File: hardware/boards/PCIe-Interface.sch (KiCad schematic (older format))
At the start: 0 parts

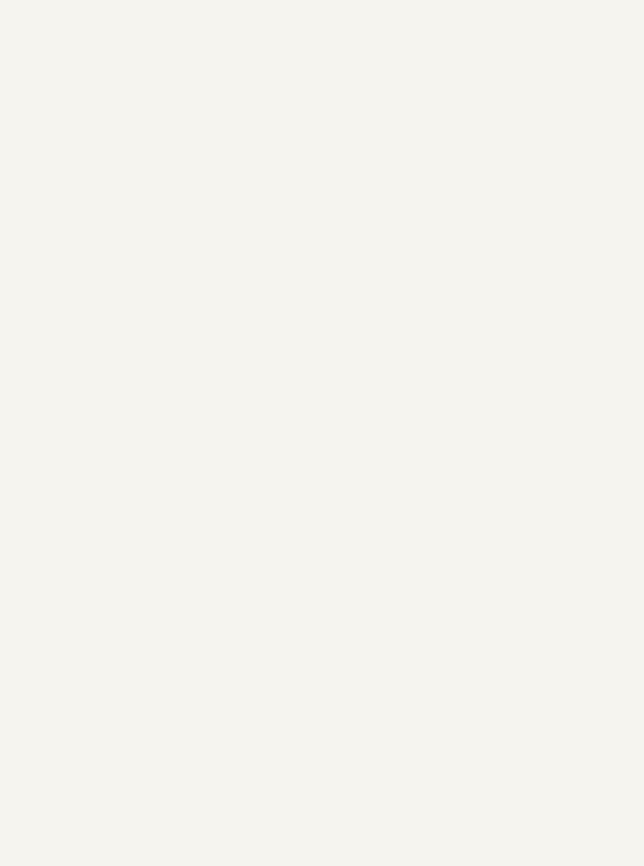
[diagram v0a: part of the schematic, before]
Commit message: Added some more schematics for blocking things out, and tweaked the GND fingers on the PCIe edge a bit
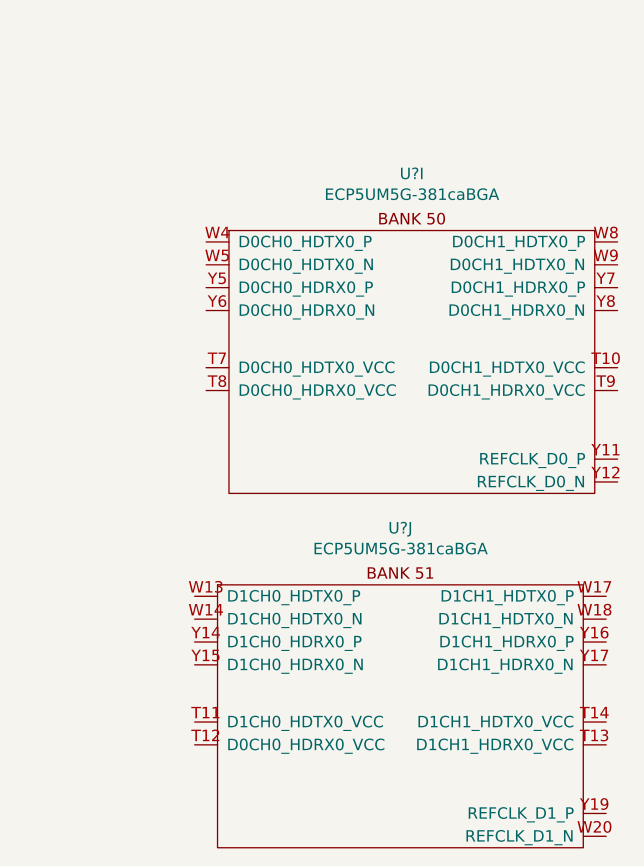
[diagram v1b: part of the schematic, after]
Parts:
- added U? (x2): ECP5UM5G-381caBGA, symbol lethalbit:ECP5UM5G-381caBGA
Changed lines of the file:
@@
 $Descr A4 11693 8268
 encoding utf-8
-Sheet 2 2
+Sheet 2 11
 Title ""
 Date ""
@@
 Text HLabel 1300 3450 0    50   Input ~ 0
 RX3_N
+$Comp
+L lethalbit:ECP5UM5G-381caBGA U?
+U 9 1 5F0889A2
+P 6050 2300
+F 0 "U?" H 6050 2648 50  0000 C CNN
+F 1 "ECP5UM5G-381caBGA" H 6050 2557 50  0000 C CNN
+F 2 "" H 4700 2450 50  0001 C CNN
+F 3 "" H 4700 2450 50  0001 C CNN
+	9    6050 2300
+	1    0    0    -1
+$EndComp
+$Comp
+L lethalbit:ECP5UM5G-381caBGA U?
+U 10 1 5F0889A8
+P 6000 3850
+F 0 "U?" H 6000 4198 50  0000 C CNN
+F 1 "ECP5UM5G-381caBGA" H 6000 4107 50  0000 C CNN
+F 2 "" H 4650 4000 50  0001 C CNN
+F 3 "" H 4650 4000 50  0001 C CNN
+	10   6000 3850
+	1    0    0    -1
+$EndComp
 $EndSCHEMATC

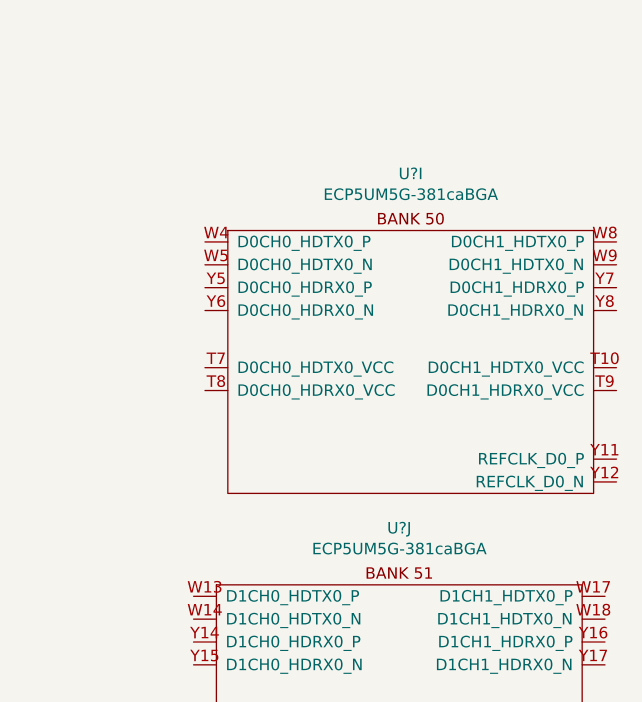
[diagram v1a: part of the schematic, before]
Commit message: Did some annotation and fixed the FPGA bank that was accidentally labled as the cypress part
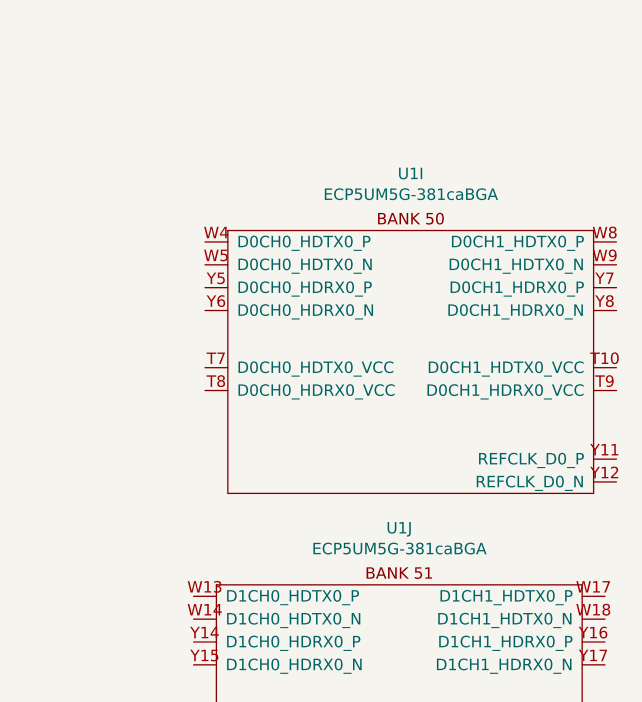
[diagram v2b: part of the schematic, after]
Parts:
- U1: renamed from U?; footprint (none) -> lethalbit:318caBGA
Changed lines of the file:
@@
 RX3_N
 $Comp
-L lethalbit:ECP5UM5G-381caBGA U?
+L lethalbit:ECP5UM5G-381caBGA U1
 U 9 1 5F0889A2
 P 6050 2300
-F 0 "U?" H 6050 2648 50  0000 C CNN
+F 0 "U1" H 6050 2648 50  0000 C CNN
 F 1 "ECP5UM5G-381caBGA" H 6050 2557 50  0000 C CNN
-F 2 "" H 4700 2450 50  0001 C CNN
+F 2 "lethalbit:318caBGA" H 4700 2450 50  0001 C CNN
 F 3 "" H 4700 2450 50  0001 C CNN
 	9    6050 2300
@@
 $EndComp
 $Comp
-L lethalbit:ECP5UM5G-381caBGA U?
+L lethalbit:ECP5UM5G-381caBGA U1
 U 10 1 5F0889A8
 P 6000 3850
-F 0 "U?" H 6000 4198 50  0000 C CNN
+F 0 "U1" H 6000 4198 50  0000 C CNN
 F 1 "ECP5UM5G-381caBGA" H 6000 4107 50  0000 C CNN
-F 2 "" H 4650 4000 50  0001 C CNN
+F 2 "lethalbit:318caBGA" H 4650 4000 50  0001 C CNN
 F 3 "" H 4650 4000 50  0001 C CNN
 	10   6000 3850

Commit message: Some strugglebusting on getting the ERC errors cleaned up a bit
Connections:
- no-connect marks 0 -> 46
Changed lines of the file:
@@
 	1    0    0    -1
 $EndComp
+NoConn ~ 1300 800
+NoConn ~ 1300 950
+NoConn ~ 1300 1400
+NoConn ~ 1300 1500
+NoConn ~ 1300 1650
+NoConn ~ 1300 1750
+NoConn ~ 1300 1900
+NoConn ~ 1300 2000
+NoConn ~ 1300 2150
+NoConn ~ 1300 2250
+NoConn ~ 1300 2500
+NoConn ~ 1300 2600
+NoConn ~ 1300 2750
+NoConn ~ 1300 2850
+NoConn ~ 1300 3000
+NoConn ~ 1300 3100
+NoConn ~ 1300 3350
+NoConn ~ 1300 3450
+NoConn ~ 5150 2250
+NoConn ~ 5150 2350
+NoConn ~ 5150 2450
+NoConn ~ 5150 2550
+NoConn ~ 5150 2800
+NoConn ~ 5150 2900
+NoConn ~ 5100 3800
+NoConn ~ 5100 3900
+NoConn ~ 5100 4000
+NoConn ~ 5100 4100
+NoConn ~ 5100 4350
+NoConn ~ 5100 4450
+NoConn ~ 6900 3800
+NoConn ~ 6900 3900
+NoConn ~ 6900 4000
+NoConn ~ 6900 4100
+NoConn ~ 6900 4350
+NoConn ~ 6900 4450
+NoConn ~ 6900 4750
+NoConn ~ 6900 4850
+NoConn ~ 6950 3300
+NoConn ~ 6950 3200
+NoConn ~ 6950 2900
+NoConn ~ 6950 2800
+NoConn ~ 6950 2550
+NoConn ~ 6950 2450
+NoConn ~ 6950 2350
+NoConn ~ 6950 2250
 $EndSCHEMATC
